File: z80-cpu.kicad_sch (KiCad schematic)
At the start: 22 parts, among them J1 RC2014_Bus, J3 Conn_02x09_Odd_Even, Q1 2N3904-AP, SW1 SW_Push, U1 Z80CPU, U2 NE555P, U3 74LS393, X1 ACO-7.3728MHz

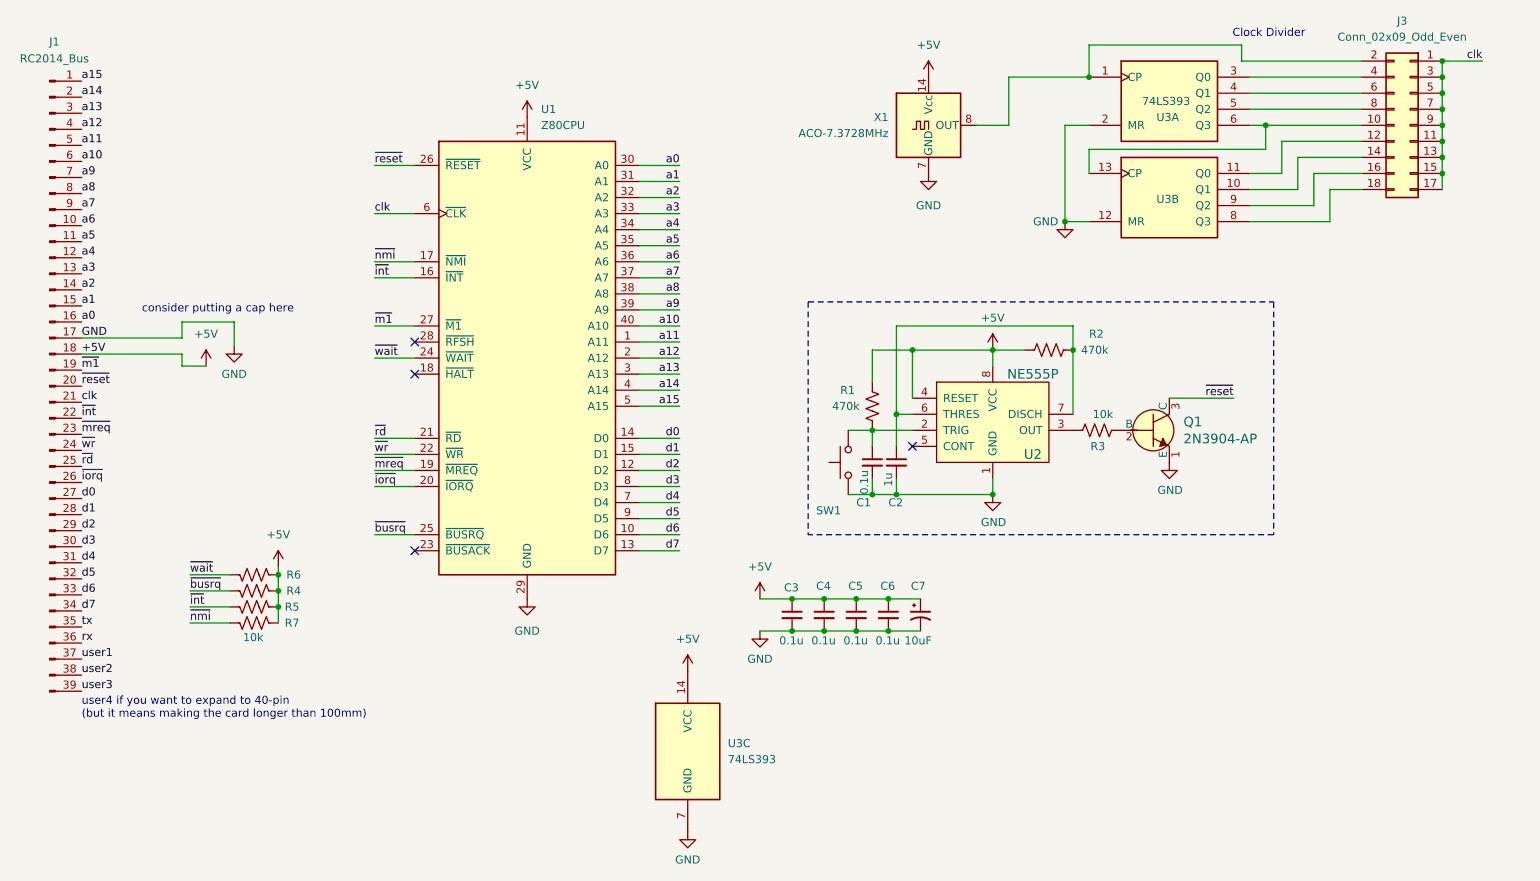
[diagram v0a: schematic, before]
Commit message: Changed bus labels to global labels, made uppercase
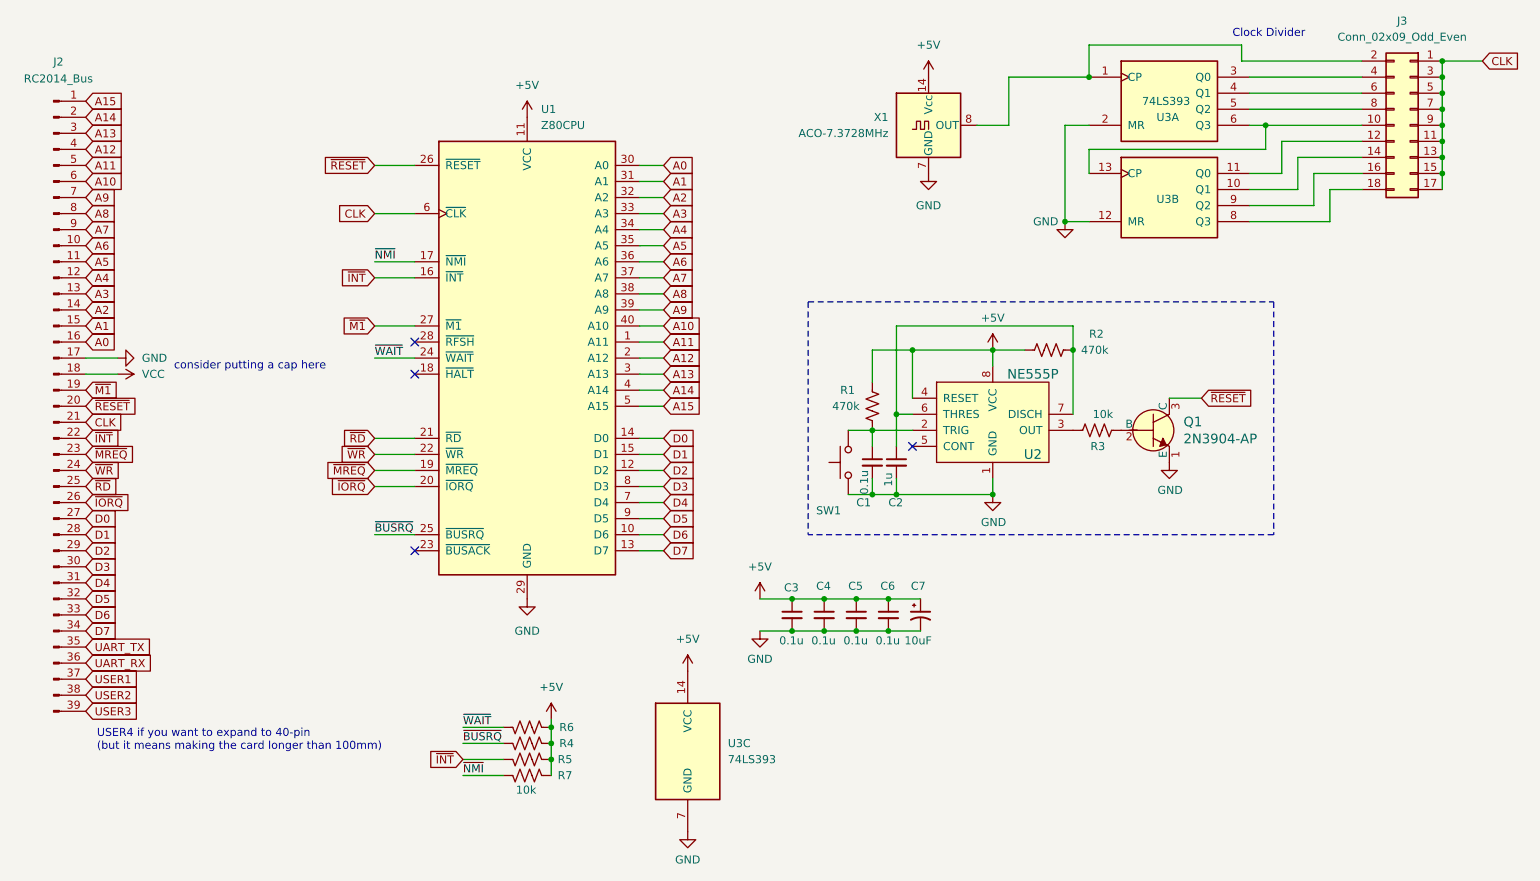
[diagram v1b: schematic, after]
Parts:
- removed J1: RC2014_Bus, Connector_PinHeader_2.54mm:PinHeader_1x39_P2.54mm_Vertical, symbol Connector:Conn_01x39_Pin
- added J2: RC2014_Bus, Connector_PinHeader_2.54mm:PinHeader_1x39_P2.54mm_Vertical, symbol Connector:Conn_01x39_Pin
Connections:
- net GND: now also J2.17 (Pin_17)
- net a0 renamed A0
- net A0: now also J2.16 (Pin_16)
- net a1 renamed A1
- net A1: now also J2.15 (Pin_15)
- net a10 renamed A10
- net A10: now also J2.6 (Pin_6)
- net a11 renamed A11
- net A11: now also J2.5 (Pin_5)
- net a12 renamed A12
- net A12: now also J2.4 (Pin_4)
- net a13 renamed A13
- net A13: now also J2.3 (Pin_3)
- net a14 renamed A14
- net A14: now also J2.2 (Pin_2)
- net a15 renamed A15
- net A15: now also J2.1 (Pin_1)
- net a2 renamed A2
- net A2: now also J2.14 (Pin_14)
- net a3 renamed A3
- net A3: now also J2.13 (Pin_13)
- net a4 renamed A4
- net A4: now also J2.12 (Pin_12)
- net a5 renamed A5
- net A5: now also J2.11 (Pin_11)
- net a6 renamed A6
- net A6: now also J2.10 (Pin_10)
- net a7 renamed A7
- net A7: now also J2.9 (Pin_9)
- net a8 renamed A8
- net A8: now also J2.8 (Pin_8)
- net a9 renamed A9
- net A9: now also J2.7 (Pin_7)
- net clk renamed CLK
- net CLK: now also J2.21 (Pin_21)
- net d0 renamed D0
- net D0: now also J2.27 (Pin_27)
- net d1 renamed D1
- net D1: now also J2.28 (Pin_28)
- net d2 renamed D2
- net D2: now also J2.29 (Pin_29)
- net d3 renamed D3
- net D3: now also J2.30 (Pin_30)
- net d4 renamed D4
- net D4: now also J2.31 (Pin_31)
- net d5 renamed D5
- net D5: now also J2.32 (Pin_32)
- net d6 renamed D6
- net D6: now also J2.33 (Pin_33)
- net d7 renamed D7
- net D7: now also J2.34 (Pin_34)
- net ~{busrq} renamed ~{BUSRQ}
- net ~{int} renamed ~{INT}
- net ~{INT}: now also J2.22 (Pin_22)
- net ~{iorq} renamed ~{IORQ}
- net ~{IORQ}: now also J2.26 (Pin_26)
- net ~{m1} renamed ~{M1}
- net ~{M1}: now also J2.19 (Pin_19)
- net ~{mreq} renamed ~{MREQ}
- net ~{MREQ}: now also J2.23 (Pin_23)
- net ~{nmi} renamed ~{NMI}
- net ~{rd} renamed ~{RD}
- net ~{RD}: now also J2.25 (Pin_25)
- net ~{reset} renamed ~{RESET}
- net ~{RESET}: now also J2.20 (Pin_20)
- net ~{wait} renamed ~{WAIT}
- net ~{wr} renamed ~{WR}
- net ~{WR}: now also J2.24 (Pin_24)
- new net UART_RX: J2.36 (Pin_36)
- new net UART_TX: J2.35 (Pin_35)
- new net USER1: J2.37 (Pin_37)
- new net USER2: J2.38 (Pin_38)
- new net USER3: J2.39 (Pin_39)
- new net VCC: J2.18 (Pin_18)
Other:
- note added: "USER4 if you want to expand to 40-pin (but it means making the card longer than 100mm)"
- note removed: "user4 if you want to expand to 40-pin (but it means making the card longer than 100mm)"
- moved on the sheet: R4, R5, R6, R7

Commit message: Fixed missing reset pullup, and slightly broken schematic after changing header labels. Rev 2
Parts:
- added R4: 10k, Resistor_THT:R_Axial_DIN0207_L6.3mm_D2.5mm_P10.16mm_Horizontal, symbol Device:R_US
- SW1: value SW_Push -> RESET
- U2: value NE555P -> NE555
- U3: value 74LS393 -> 74HCT393
- renumbered J2 to J1, R4 to R5, R5 to R6, R6 to R7, R7 to R8
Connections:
- net +5V is gone; now on net VCC: C3.1, C4.1, C5.1, C6.1, C7.1, R1.1, R2.2, R5.1, R6.1, R7.1, R8.1, U1.11 (VCC), U2.4 (RESET), U2.8 (VCC), U3.14 (VCC), X1.14 (Vcc)
- net VCC: now also R4.1
- net ~{RESET}: now also R4.2
